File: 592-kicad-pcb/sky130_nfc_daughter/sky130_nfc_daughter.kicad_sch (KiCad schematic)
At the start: 81 parts, among them J1 U.FL-R-SMT-1_80_, J10 U.FL-R-SMT-1_80_, J2 U.FL-R-SMT-1_80_, J3 U.FL-R-SMT-1_80_, J4 U.FL-R-SMT-1_80_, J5 U.FL-R-SMT-1_80_, J6 U.FL-R-SMT-1_80_, J7 U.FL-R-SMT-1_80_, J8 DF40C-40DS-0.4V_51_, J9 DF40C-40DS-0.4V_51_, U1 Caravel_QFN, U3 W25Q32JVZP

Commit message: add 3D models with rel paths, add stitching via footprint, update daughter pcb schematic
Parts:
- added C29: C_1u_0603_50V, Capacitor_SMD:C_0603_1608Metric, symbol Device:C
- added D10, D9: SMAJ10CA, Diode_SMD:D_SMA, symbol Diode:SMAJ10CA
- added D4: PESD3V3S1UL, Diode_SMD:D_SOD-882, symbol Diode:PESD3V3S1UL
- added R6, R7, R8: 0, Resistor_SMD:R_0402_1005Metric, symbol Device:R
- added SW1: SW_Push, Button_Switch_SMD:SW_Push_1P1T_XKB_TS-1187A, symbol Switch:SW_Push
- C1, C10, C14, C18, C19, C2, C20, C21, C23, C24, C25: symbol psypassives:C_1u_0603_50V -> Device:C
- C15, C16, C17, C26, C28, C31, L3, L4, R11, R12: now not fitted
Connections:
- net ANA_MUX_OUT_2_EXT: now also D10.2 (A2)
- net ANA_MUX_OUT_EXT: now also D9.2 (A2); no longer J8.34
- net GND: now also C29.2, D10.1 (A1), D4.2 (A), D9.1 (A1), SW1.1; no longer C15.1, C17.2, C26.2, C31.1
- net J_ANA_MUX_OUT_EXT: now also J8.34
- net NFC_AFE_TDO_EXT: now also D4.1 (K)
- net VRECT_OUT_EXT: now also C29.1
- net flash_clk: now also R6.2; no longer U3.6 (CLK)
- net flash_io0: now also R7.2; no longer U3.5 (DI/IO_{0})
- net flash_io1: now also R8.2; no longer U3.2 (DO/IO_{1})
- net flash_rstb: now also SW1.2
- new net: R7.1, U3.5 (DI/IO_{0})
- new net: R8.1, U3.2 (DO/IO_{1})
- new net: R6.1, U3.6 (CLK)
- new net: C15.1, C17.2, C26.2, C31.1
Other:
- note added: "2x20 headers mezzanine, bottom side, 34mm separation center to center"
- note added: "Bulk Capacitance"
- note added: "ESD Protection (10V)"
- note added: "Flash Memory (4MiB)"
- note added: "NFC Matching Network"
- note added: "NFC Sky130nm"
- note removed: "2x20 headers, bottom side, 40mm separation"
- note removed: "ADD RESET BUTTON"
- moved on the sheet: C1, C10, C11, C12, C13, C14, C18, C19, C2, C20, C21, C22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

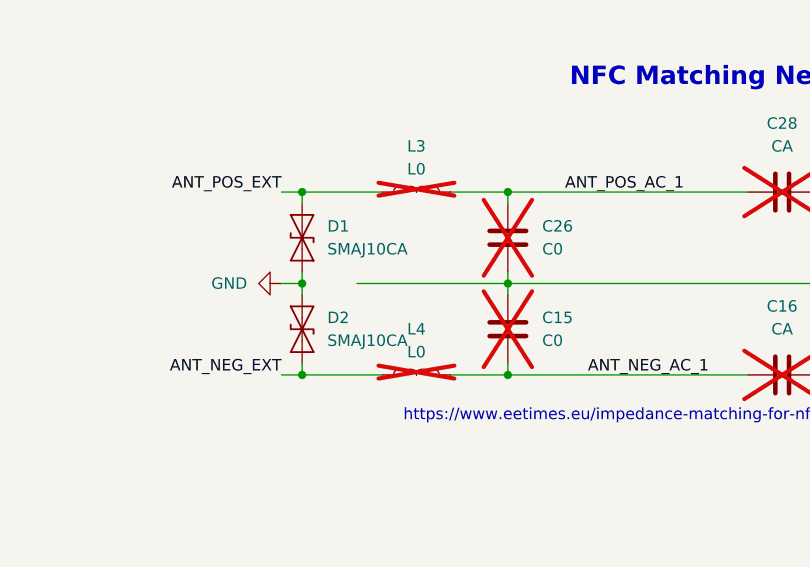
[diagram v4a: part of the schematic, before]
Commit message: begin routing daughterboard
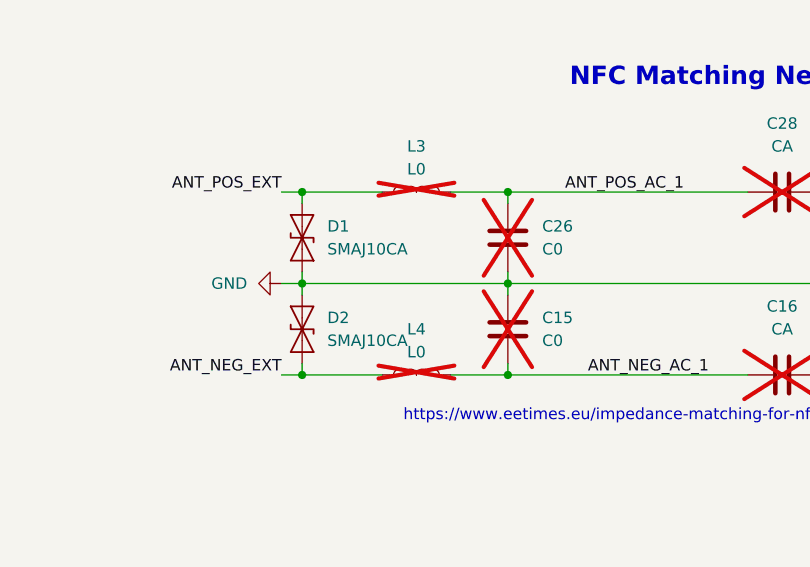
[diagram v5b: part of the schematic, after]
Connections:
- net GND: now also C15.1, C17.2, C26.2, C31.1
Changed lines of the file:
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@@
+	(wire
+		(pts
+			(xy 288.29 207.01) (xy 311.15 207.01)
+		)
+		(stroke
+			(width 0)
+			(type default)
+		)
+	)
 	(wire
 		(pts
@@
 		)
 		(stroke
-			(width 0)
-			(type default)
-		)
-	)
-	(wire
-		(pts
-			(xy 294.386 207.01) (xy 311.15 207.01)
-		)
-		(stroke

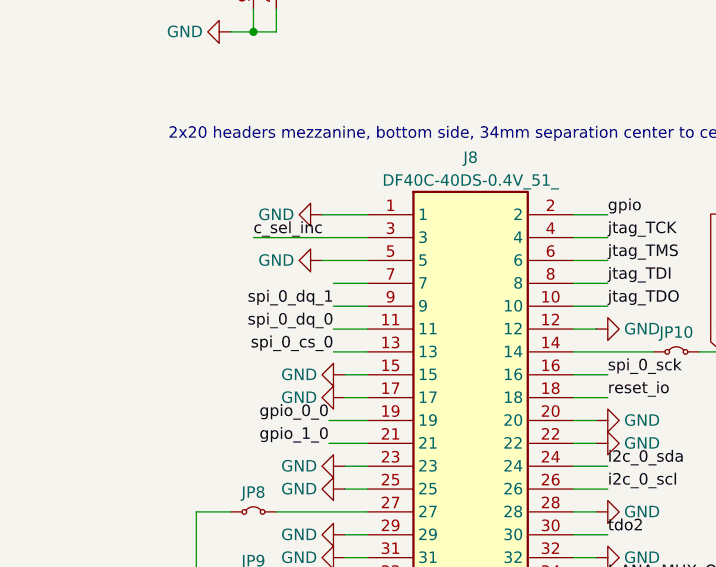
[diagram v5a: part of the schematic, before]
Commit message: clean up schematics, add proper connectors
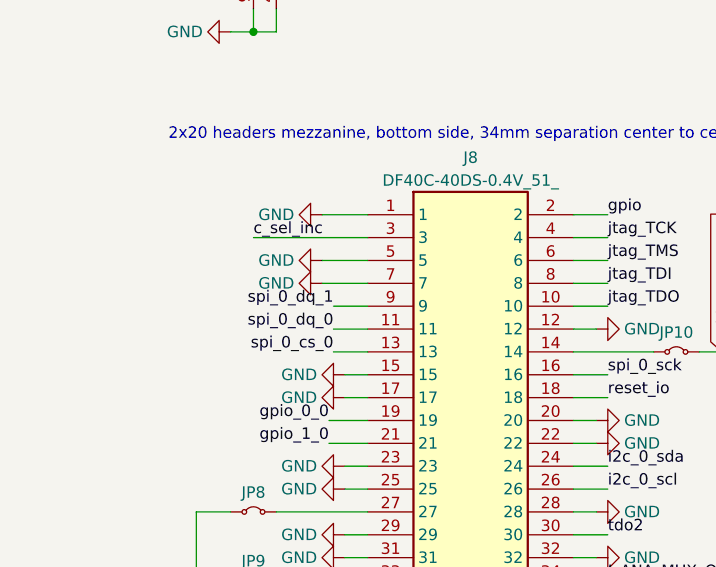
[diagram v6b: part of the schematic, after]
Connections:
- net GND: now also J8.7
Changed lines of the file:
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@@
 	(wire
 		(pts
-			(xy 54.61 101.6) (xy 58.42 101.6)
-		)
-		(stroke
-			(width 0)
-			(type default)
-		)
-	)
-	(wire
-		(pts
 			(xy 81.28 96.52) (xy 85.09 96.52)
 		)
@@
 	(wire
 		(pts
+			(xy 53.34 101.6) (xy 58.42 101.6)
+		)
+		(stroke
+			(width 0)
+			(type default)
+		)
+	)
+	(wire
+		(pts
 			(xy 177.8 105.41) (xy 181.61 105.41)
 		)
@@
 					(unit 1)
 				)
+			)
+		)
+	)
+	(symbol
+		(lib_id "power:GND")
+		(at 53.34 101.6 270)
+		(unit 1)
+		(exclude_from_sim no)
+		(in_bom yes)
+		(on_board yes)
+		(dnp no)
+		(property "Reference" "#PWR083"
+			(at 46.99 101.6 0)
+			(effects
+				(font
+					(size 1.27 1.27)
+				)
+				(hide yes)
+			)
+		)
+		(property "Value" "GND"
+			(at 48.26 101.6 90)
+			(effects
+				(font
+					(size 1.27 1.27)
+				)
+			)
+		)
+		(property "Footprint" ""
+			(at 53.34 101.6 0)
+			(effects
+				(font
+					(size 1.27 1.27)
+				)
+				(hide yes)
+			)
+		)
+		(property "Datasheet" ""
+			(at 53.34 101.6 0)
+			(effects
+				(font
+					(size 1.27 1.27)
+				)
+				(hide yes)
+			)
+		)
+		(property "Description" "Power symbol creates a global label with name \"GND\" , ground"
+			(at 53.34 101.6 0)
+			(effects
+				(font
+					(size 1.27 1.27)
+				)
+				(hide yes)
+			)
+		)
+		(pin "1"
+		)
+		(instances
+			(project "sky130_nfc_daughter"
+				(path "/b38c65ac-2d57-46f9-9a32-ad09573ee400"
+					(reference "#PWR083")
+					(unit 1)
+				)

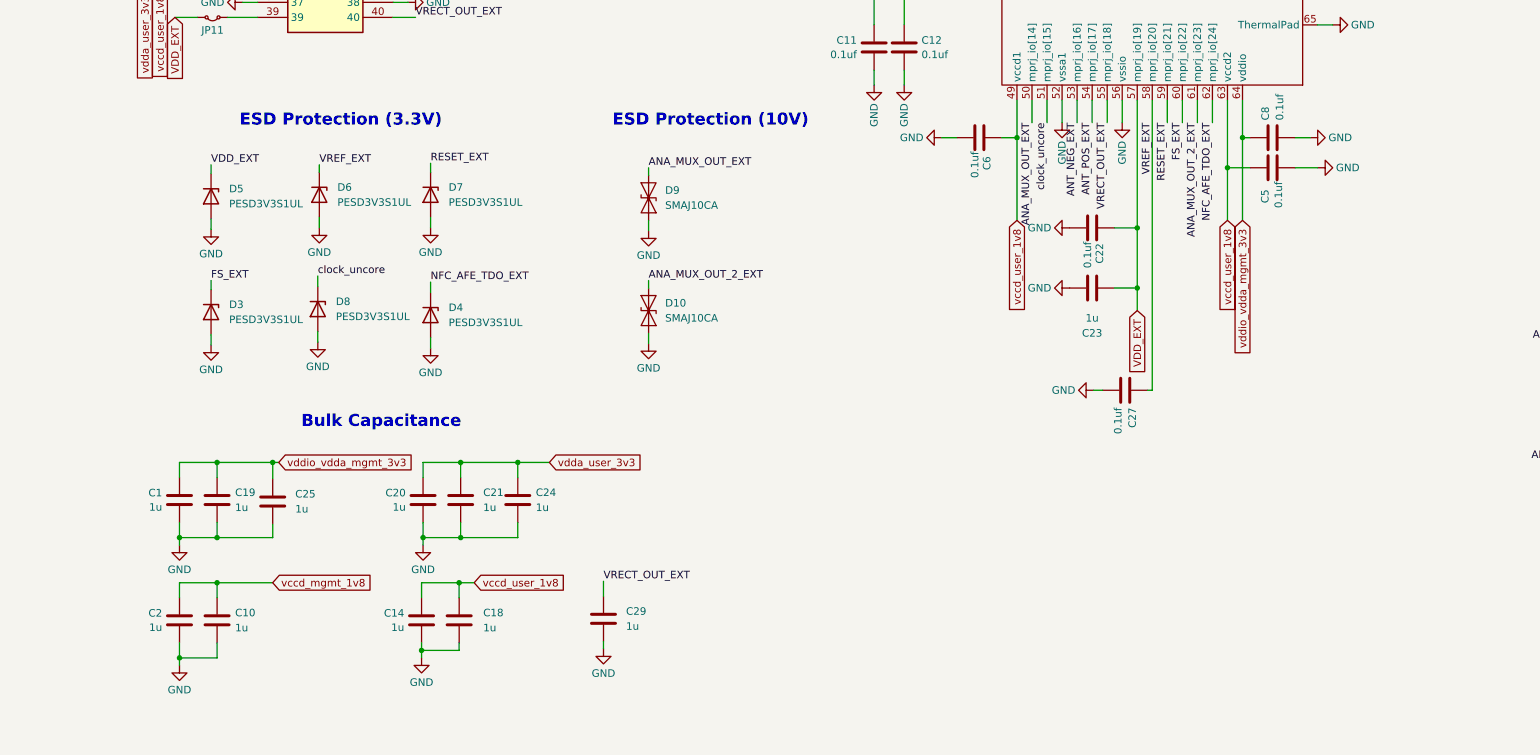
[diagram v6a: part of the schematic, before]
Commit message: add some daughterboard routing
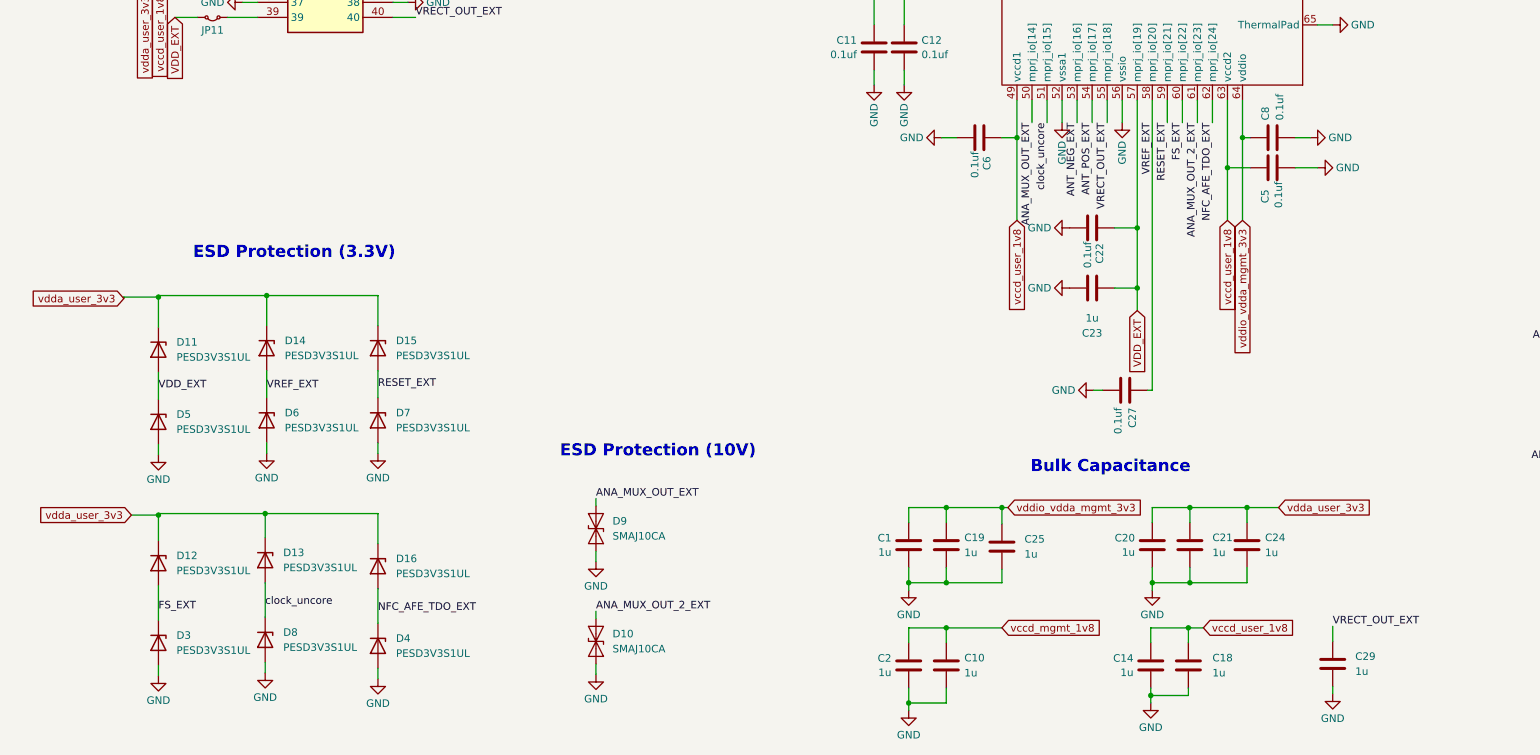
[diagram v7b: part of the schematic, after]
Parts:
- added D11, D12, D13, D14, D15, D16: PESD3V3S1UL, Diode_SMD:D_SOD-882, symbol Diode:PESD3V3S1UL
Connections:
- net FS_EXT: now also D12.2 (A)
- net NFC_AFE_TDO_EXT: now also D16.2 (A)
- net RESET_EXT: now also D15.2 (A)
- net VDD_EXT: now also D11.2 (A)
- net VREF_EXT: now also D14.2 (A)
- net clock_uncore: now also D13.2 (A)
- net vdda_user_3v3: now also D11.1 (K), D12.1 (K), D13.1 (K), D14.1 (K), D15.1 (K), D16.1 (K)
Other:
- moved on the sheet: C1, C10, C14, C18, C19, C2, C20, C21, C24, C25, C29, D10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

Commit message: daughterboard routing, changed some mezzanine pins - more to come
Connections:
- net c_sel_inc is gone; now on net GND: J8.3
- net GND: now also J8.16, J8.18, J8.24, J8.26, J8.30, J9.11, J9.13, J9.15, J9.17, J9.19, J9.27, J9.5, J9.7, J9.9; no longer J8.15, J8.17, J8.23, J8.25, J8.29, J9.10, J9.12, J9.14, J9.16, J9.18, J9.24, J9.30, J9.6, J9.8
- net J_FS_EXT: now also J9.31; no longer J9.32
- net J_clk: now also J9.6; no longer J9.5
- net J_ext_clk_dig: now also J9.22; no longer J9.20
- net RESET_EXT: now also J9.29; no longer J9.34
- net TCK_EXT: now also J9.32; no longer J9.29
- net TMS_EXT: now also J9.30; no longer J9.27
- net TRST_EXT: now also J9.34; no longer J9.31
- net ext_reset_dig: now also J9.24; no longer J9.22
- net gpio: now also J8.10; no longer J8.2
- net i2c_0_scl: now also J8.25; no longer J8.26
- net i2c_0_sda: now also J8.23; no longer J8.24
- net jtag_TCK: now also J8.8; no longer J8.4
- net jtag_TDI: now also J8.4; no longer J8.8
- net jtag_TDO: now also J8.2; no longer J8.10
- net reset_b: now also J9.8; no longer J9.7
- net reset_io: now also J8.17; no longer J8.18
- net spi_0_sck: now also J8.15; no longer J8.16
- net spi_flash_0_cs_0: now also J9.18; no longer J9.17
- net spi_flash_0_dq_0: now also J9.16; no longer J9.15
- net spi_flash_0_dq_1: now also J9.14; no longer J9.13
- net spi_flash_0_dq_2: now also J9.12; no longer J9.11
- net spi_flash_0_dq_3: now also J9.10; no longer J9.9
- net spi_flash_0_sck: now also J9.20; no longer J9.19
- net tdo2: now also J8.29; no longer J8.30
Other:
- moved on the sheet: J8, J9, JP10, JP11, JP6, JP7, JP8, JP9, TP1, TP2, TP3, TP4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
